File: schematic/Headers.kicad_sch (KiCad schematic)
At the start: 0 parts

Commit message: Create FPGA schematic
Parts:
- added J4: Header 1, Connector_PinHeader_2.54mm:PinHeader_1x16_P2.54mm_Vertical, symbol Connector_Generic:Conn_01x16
- added J5: Header 2, Connector_PinHeader_2.54mm:PinHeader_1x16_P2.54mm_Vertical, symbol Connector_Generic:Conn_01x16
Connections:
- new net IO0: J4.1 (Pin_1)
- new net IO13: J4.9 (Pin_9)
- new net IO16: J4.10 (Pin_10)
- new net IO18: J4.11 (Pin_11)
- new net IO2: J4.2 (Pin_2)
- new net IO20: J4.12 (Pin_12)
- new net IO22: J4.13 (Pin_13)
- new net IO23: J4.14 (Pin_14)
- new net IO24: J4.15 (Pin_15)
- new net IO25: J4.16 (Pin_16)
- new net IO29: J5.1 (Pin_1)
- new net IO3: J4.3 (Pin_3)
- new net IO31: J5.2 (Pin_2)
- new net IO36: J5.3 (Pin_3)
- new net IO37: J5.4 (Pin_4)
- new net IO38: J5.5 (Pin_5)
- new net IO39: J5.6 (Pin_6)
- new net IO4: J4.4 (Pin_4)
- new net IO41: J5.7 (Pin_7)
- new net IO42: J5.8 (Pin_8)
- new net IO43: J5.9 (Pin_9)
- new net IO44: J5.10 (Pin_10)
- new net IO45: J5.11 (Pin_11)
- new net IO46: J5.12 (Pin_12)
- new net IO48: J5.13 (Pin_13)
- new net IO49: J5.14 (Pin_14)
- new net IO5: J4.5 (Pin_5)
- new net IO50: J5.15 (Pin_15)
- new net IO51: J5.16 (Pin_16)
- new net IO6: J4.6 (Pin_6)
- new net IO8: J4.7 (Pin_7)
- new net IO9: J4.8 (Pin_8)
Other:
- title: (none) -> iCE40 DevBoard

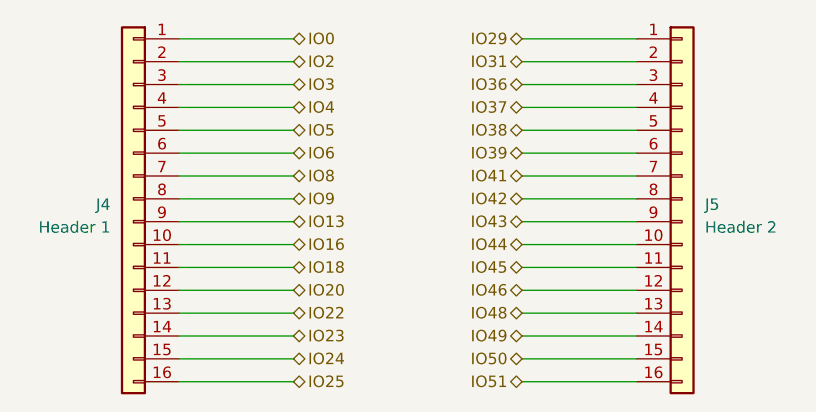
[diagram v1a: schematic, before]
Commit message: Update flash header schematic
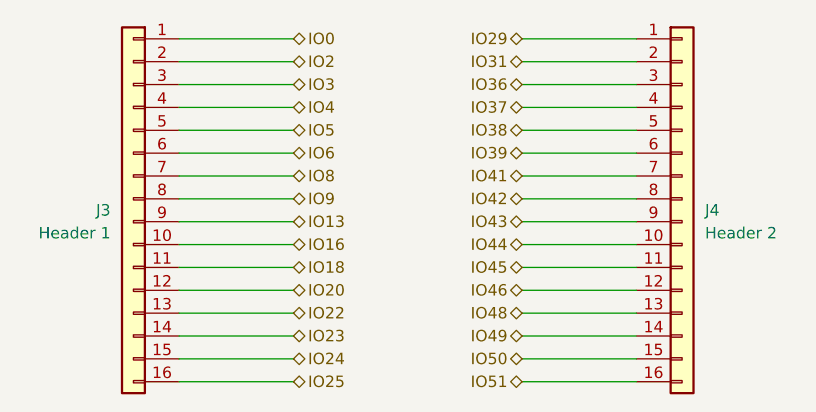
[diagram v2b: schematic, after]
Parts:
- renumbered J4 to J3, J5 to J4
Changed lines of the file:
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@@
   )
   (symbol (lib_id "Connector_Generic:Conn_01x16") (at 182.88 93.98 0) (unit 1)
-    (in_bom yes) (on_board yes) (dnp no) (fields_autoplaced)
-    (property "Reference" "J5" (at 185.42 94.615 0)
+    (in_bom yes) (on_board yes) (dnp no)
+    (property "Reference" "J4" (at 185.42 95.25 0)
       (effects (font (size 1.27 1.27)) (justify left))
     )
-    (property "Value" "Header 2" (at 185.42 97.155 0)
+    (property "Value" "Header 2" (at 185.42 97.79 0)
       (effects (font (size 1.27 1.27)) (justify left))
     )
@@
       (project "iCE40DevBoard"
         (path "/2f10ad52-4a2c-425a-8339-df6126e31315/19593465-3760-482e-82bf-cb43b444c11c"
-          (reference "J5") (unit 1)
+          (reference "J4") (unit 1)
         )
       )
@@
   )
   (symbol (lib_id "Connector_Generic:Conn_01x16") (at 121.92 93.98 0) (mirror y) (unit 1)
-    (in_bom yes) (on_board yes) (dnp no) (fields_autoplaced)
-    (property "Reference" "J4" (at 119.38 94.615 0)
+    (in_bom yes) (on_board yes) (dnp no)
+    (property "Reference" "J3" (at 119.38 95.25 0)
       (effects (font (size 1.27 1.27)) (justify left))
     )
-    (property "Value" "Header 1" (at 119.38 97.155 0)
+    (property "Value" "Header 1" (at 119.38 97.79 0)
       (effects (font (size 1.27 1.27)) (justify left))
     )
@@
       (project "iCE40DevBoard"
         (path "/2f10ad52-4a2c-425a-8339-df6126e31315/19593465-3760-482e-82bf-cb43b444c11c"
-          (reference "J4") (unit 1)
+          (reference "J3") (unit 1)
         )
       )
